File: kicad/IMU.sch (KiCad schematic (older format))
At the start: 3 parts, among them U6 ICM-20602

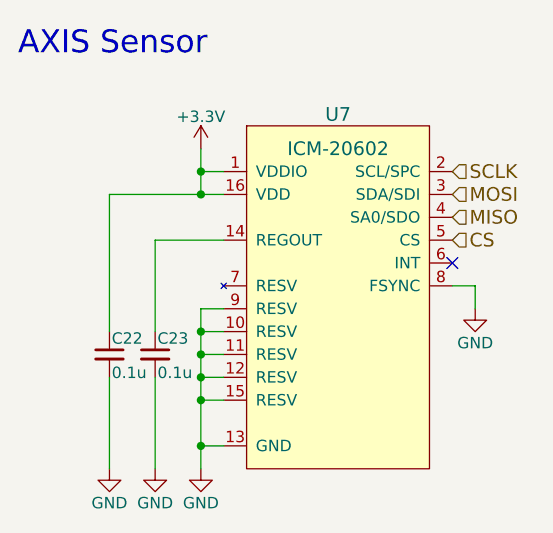
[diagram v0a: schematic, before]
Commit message: 部品を配置
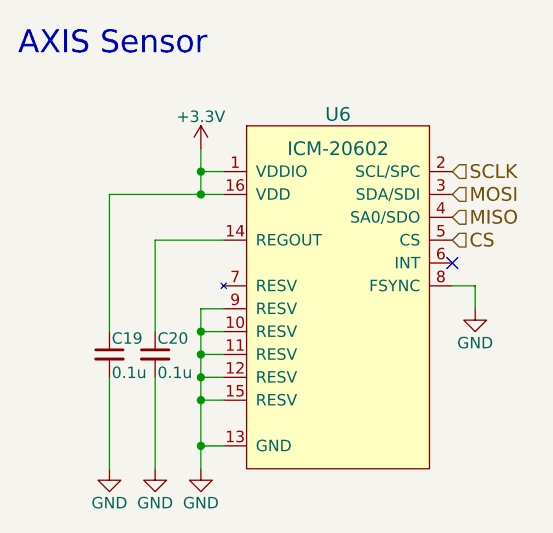
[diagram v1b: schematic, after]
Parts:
- renumbered C16 to C19, C17 to C20
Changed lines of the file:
@@
 EESchema Schematic File Version 4
 LIBS:KERISE-cache
-EELAYER 26 0
+EELAYER 29 0
 EELAYER END
 $Descr A4 11693 8268
 encoding utf-8
-Sheet 13 15
+Sheet 10 13
 Title ""
 Date ""
@@
 AXIS Sensor
 $Comp
-L KERISE:ICM-20602 U6
+L KERISE:ICM-20602 U?
 U 1 1 592C611A
 P 5600 3400
-AR Path="/57CC33F6/592C611A" Ref="U6"  Part="1"
-AR Path="/5A18D4D6/592C611A" Ref="U7"  Part="1"
-F 0 "U7" H 5600 4150 60  0000 C CNN
+AR Path="/57CC33F6/592C611A" Ref="U?"  Part="1"
+AR Path="/5A18D4D6/592C611A" Ref="U6"  Part="1"
+F 0 "U6" H 5600 4150 60  0000 C CNN
 F 1 "ICM-20602" H 5600 4000 60  0000 C CNN
 F 2 "mouse:ICM-20602" H 5600 4000 60  0001 C CNN
@@
 $EndComp
 $Comp
-L Device:C_Small C17
+L Device:C_Small C?
 U 1 1 592C613A
 P 4800 3700
-AR Path="/57CC33F6/592C613A" Ref="C17"  Part="1"
-AR Path="/5A18D4D6/592C613A" Ref="C23"  Part="1"
-F 0 "C23" H 4810 3770 50  0000 L CNN
+AR Path="/57CC33F6/592C613A" Ref="C?"  Part="1"
+AR Path="/5A18D4D6/592C613A" Ref="C20"  Part="1"
+F 0 "C20" H 4810 3770 50  0000 L CNN
 F 1 "0.1u" H 4810 3620 50  0000 L CNN
 F 2 "Capacitor_SMD:C_0201_0603Metric" H 4800 3700 50  0001 C CNN
@@
 $EndComp
 $Comp
-L Device:C_Small C16
+L Device:C_Small C?
 U 1 1 592C6186
 P 4600 3700
-AR Path="/57CC33F6/592C6186" Ref="C16"  Part="1"
-AR Path="/5A18D4D6/592C6186" Ref="C22"  Part="1"
-F 0 "C22" H 4610 3770 50  0000 L CNN
+AR Path="/57CC33F6/592C6186" Ref="C?"  Part="1"
+AR Path="/5A18D4D6/592C6186" Ref="C19"  Part="1"
+F 0 "C19" H 4610 3770 50  0000 L CNN
 F 1 "0.1u" H 4610 3620 50  0000 L CNN
 F 2 "Capacitor_SMD:C_0201_0603Metric" H 4600 3700 50  0001 C CNN
@@
 $EndComp
 $Comp
-L power:GND #PWR058
+L power:GND #PWR?
 U 1 1 592C63E1
 P 5000 4200
-AR Path="/57CC33F6/592C63E1" Ref="#PWR058"  Part="1"
-AR Path="/5A18D4D6/592C63E1" Ref="#PWR069"  Part="1"
-F 0 "#PWR069" H 5000 3950 50  0001 C CNN
+AR Path="/57CC33F6/592C63E1" Ref="#PWR?"  Part="1"
+AR Path="/5A18D4D6/592C63E1" Ref="#PWR059"  Part="1"
+F 0 "#PWR059" H 5000 3950 50  0001 C CNN
 F 1 "GND" H 5000 4050 50  0000 C CNN
 F 2 "" H 5000 4200 50  0000 C CNN
@@
 $EndComp
 $Comp
-L power:GND #PWR056
+L power:GND #PWR?
 U 1 1 592C640D
 P 4800 4200
-AR Path="/57CC33F6/592C640D" Ref="#PWR056"  Part="1"
-AR Path="/5A18D4D6/592C640D" Ref="#PWR067"  Part="1"
-F 0 "#PWR067" H 4800 3950 50  0001 C CNN
+AR Path="/57CC33F6/592C640D" Ref="#PWR?"  Part="1"
+AR Path="/5A18D4D6/592C640D" Ref="#PWR057"  Part="1"
+F 0 "#PWR057" H 4800 3950 50  0001 C CNN
 F 1 "GND" H 4800 4050 50  0000 C CNN
 F 2 "" H 4800 4200 50  0000 C CNN
@@
 $EndComp
 $Comp
-L power:GND #PWR055
+L power:GND #PWR?
 U 1 1 592C6444
 P 4600 4200
-AR Path="/57CC33F6/592C6444" Ref="#PWR055"  Part="1"
-AR Path="/5A18D4D6/592C6444" Ref="#PWR066"  Part="1"
-F 0 "#PWR066" H 4600 3950 50  0001 C CNN
+AR Path="/57CC33F6/592C6444" Ref="#PWR?"  Part="1"
+AR Path="/5A18D4D6/592C6444" Ref="#PWR056"  Part="1"
+F 0 "#PWR056" H 4600 3950 50  0001 C CNN
 F 1 "GND" H 4600 4050 50  0000 C CNN
 F 2 "" H 4600 4200 50  0000 C CNN
@@
 $EndComp
 $Comp
-L power:+3.3V #PWR057
+L power:+3.3V #PWR?
 U 1 1 592C64FB
 P 5000 2800
-AR Path="/57CC33F6/592C64FB" Ref="#PWR057"  Part="1"
-AR Path="/5A18D4D6/592C64FB" Ref="#PWR068"  Part="1"
-F 0 "#PWR068" H 5000 2650 50  0001 C CNN
+AR Path="/57CC33F6/592C64FB" Ref="#PWR?"  Part="1"
+AR Path="/5A18D4D6/592C64FB" Ref="#PWR058"  Part="1"
+F 0 "#PWR058" H 5000 2650 50  0001 C CNN
 F 1 "+3.3V" H 5000 2940 50  0000 C CNN
 F 2 "" H 5000 2800 50  0000 C CNN
@@
 NoConn ~ 6100 3300
 $Comp
-L power:GND #PWR059
+L power:GND #PWR?
 U 1 1 592C6B85
 P 6200 3500
-AR Path="/57CC33F6/592C6B85" Ref="#PWR059"  Part="1"
-AR Path="/5A18D4D6/592C6B85" Ref="#PWR070"  Part="1"
-F 0 "#PWR070" H 6200 3250 50  0001 C CNN
+AR Path="/57CC33F6/592C6B85" Ref="#PWR?"  Part="1"
+AR Path="/5A18D4D6/592C6B85" Ref="#PWR060"  Part="1"
+F 0 "#PWR060" H 6200 3250 50  0001 C CNN
 F 1 "GND" H 6200 3350 50  0000 C CNN
 F 2 "" H 6200 3500 50  0000 C CNN
